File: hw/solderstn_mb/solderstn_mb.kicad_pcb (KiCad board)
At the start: 4 copper layers, 160 x 221.5 mm, 411 parts, among them J1201 Conn_02x05_Odd_Even, J1202 USB_B-TE_1734346-1, J1203 DB9_Male_MountingHoles, J1204 USB_A-CUI-UJ2-AH-1-SMT, J1205 Molex_NanoFit-1x02, J1301 SJ-3571N, J1302 Conn_02x05_Odd_Even, J201 74980104400, J2101 Conn_01x02, J2102 Molex_PicoBlade-53398-0271, J2103 CES-30207-158L120-67_Molex-Pi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, J2104 CES-703116-28PM_JST-conn, J2105 CES-30207-158L120-67_Molex-Pi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, J2106 CES-703116-28PM_JST-conn, J2107 Conn_Coaxial, J301 Molex_MicroFit_30-43045-0421, J501 FFC_conn_14p, J502 FFC_conn_14p, J503 JST_S2B-PH-SM4-TB, M501 FFC_retention_clamp, M502 FFC_retention_clamp, M601 Fan_4pin, M701 Fan_4pin, M801 Fan_4pin, Q1601 DMG1013T, Q1701 DMG1013T, Q1901 DMG1013T, Q2001 DMG1013T, Q2201 DMG1012T, Q301 Si4497DY, Q302 Si4497DY, Q303 DMG1012T, Q501 DMG1012T, Q601 DMG1012T, Q701 DMG1012T, Q801 DMG1012T, SW2201 Pushbutton_SMD_TS-1102W-4316, SW2202 Pushbutton_SMD_TS-1102W-4316, U1001 TMP100, U1101 TMP100, U1201 USBLC6-2SC6, U1202 74LVC2G17gw, U1203 USBLC6-2SC6, U1401 TMUX1219, U1402 TMUX1219, U1501 AD8552ARU, U1502 INA226, U1503 TPS2HB16AQ1, U1504 INA226, U1505 74LVC1G11dck, U1506 74LVC1G11dck, U1507 74LVC1G11dck, U1601 NE556d, U1602 74LVC1G175dck, U1603 74LVC1G11dck, U1701 74LVC1G175dck, U1702 74LVC1G11dck, U1801 AD8552ARU, U1802 INA226, U1803 TPS2HB16AQ1, U1804 INA226, U1805 74LVC1G11dck, U1806 74LVC1G11dck, U1807 74LVC1G11dck, U1901 NE556d, U1902 74LVC1G175dck, U1903 74LVC1G11dck, U2001 74LVC1G175dck, U2002 74LVC1G11dck, U201 IP101GA, U202 74LVC1G126SE, U2101 Si4735-D60-GU, U2102 TS4990IDT, U2103 TS4990IDT, U2201 MCP1316T-26LE-OT, U2202 W25Q64FV, U301 TPS54332DDA, U302 TLV1117LV30DCY, U303 TLV1117LV30DCY, U304 TLV1117LV30DCY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

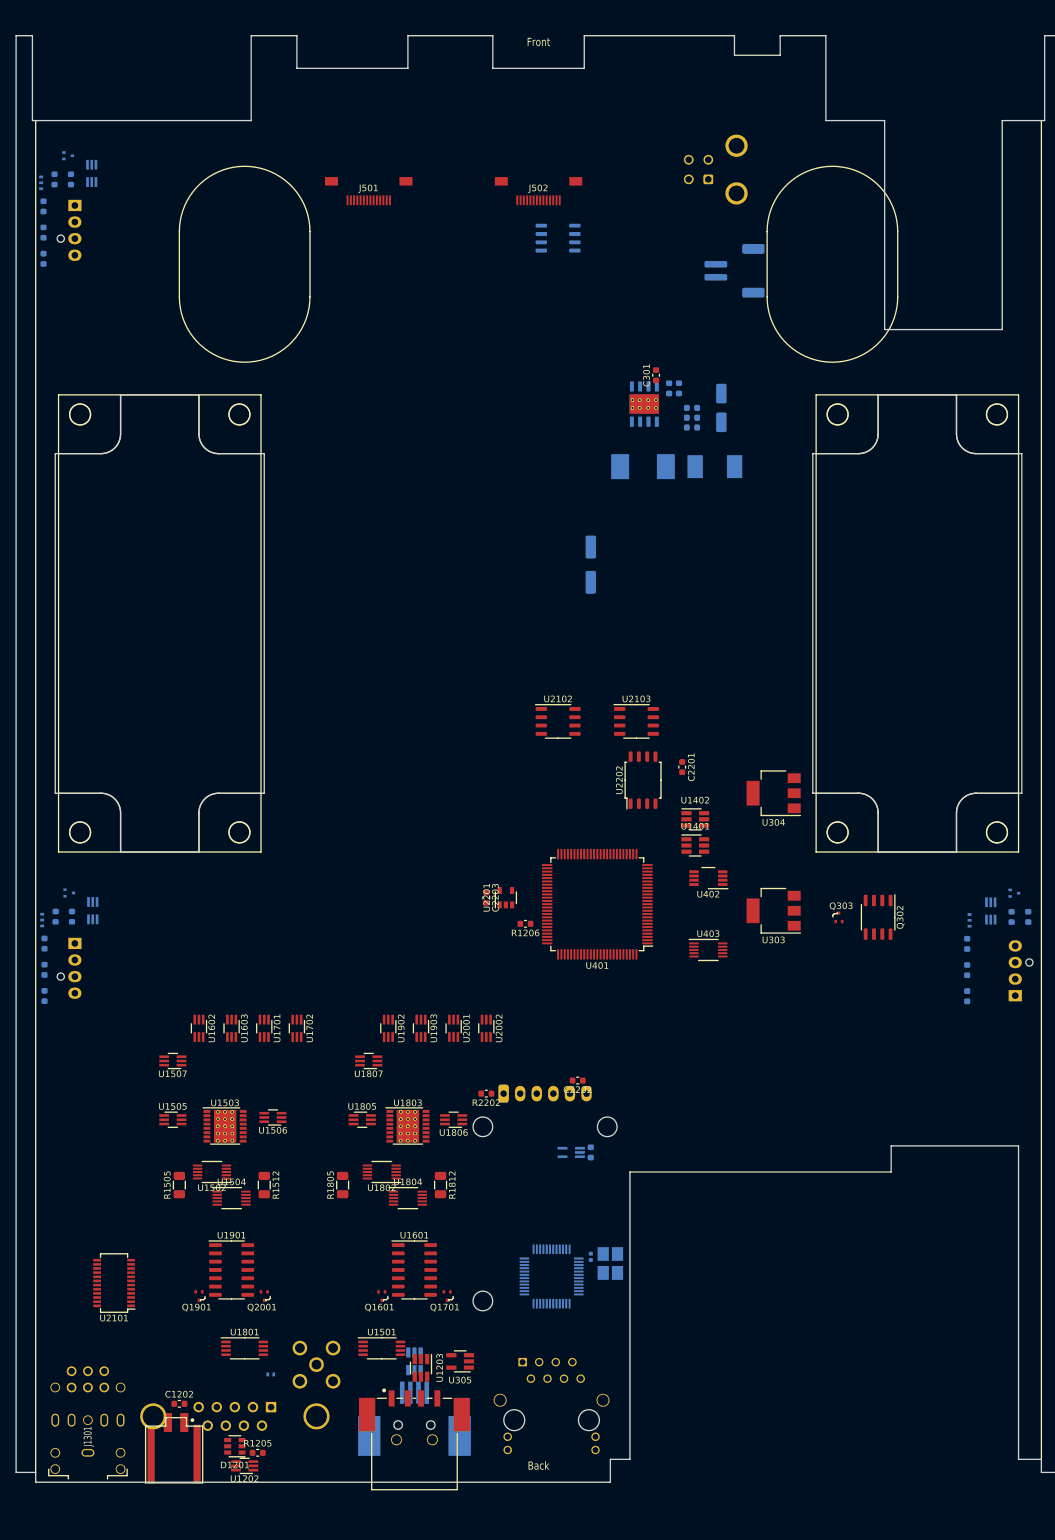
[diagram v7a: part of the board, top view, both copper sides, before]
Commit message: Rearpanel: IDC 2x5 instead of Dsub9 as dbg/bootstrp conn. Remove secondary fuseholder; rearrange DIN, P.E. banana, dbg. for more space. MainBoard: Rotate MW PSU 180deg (optimize for 230V through PwrBtn). PCB-fuse for 12V secondary side. IDC 2x5 instead of Dsub9; include DbgLED on free pin; ESD TVS on all dbgcon pins
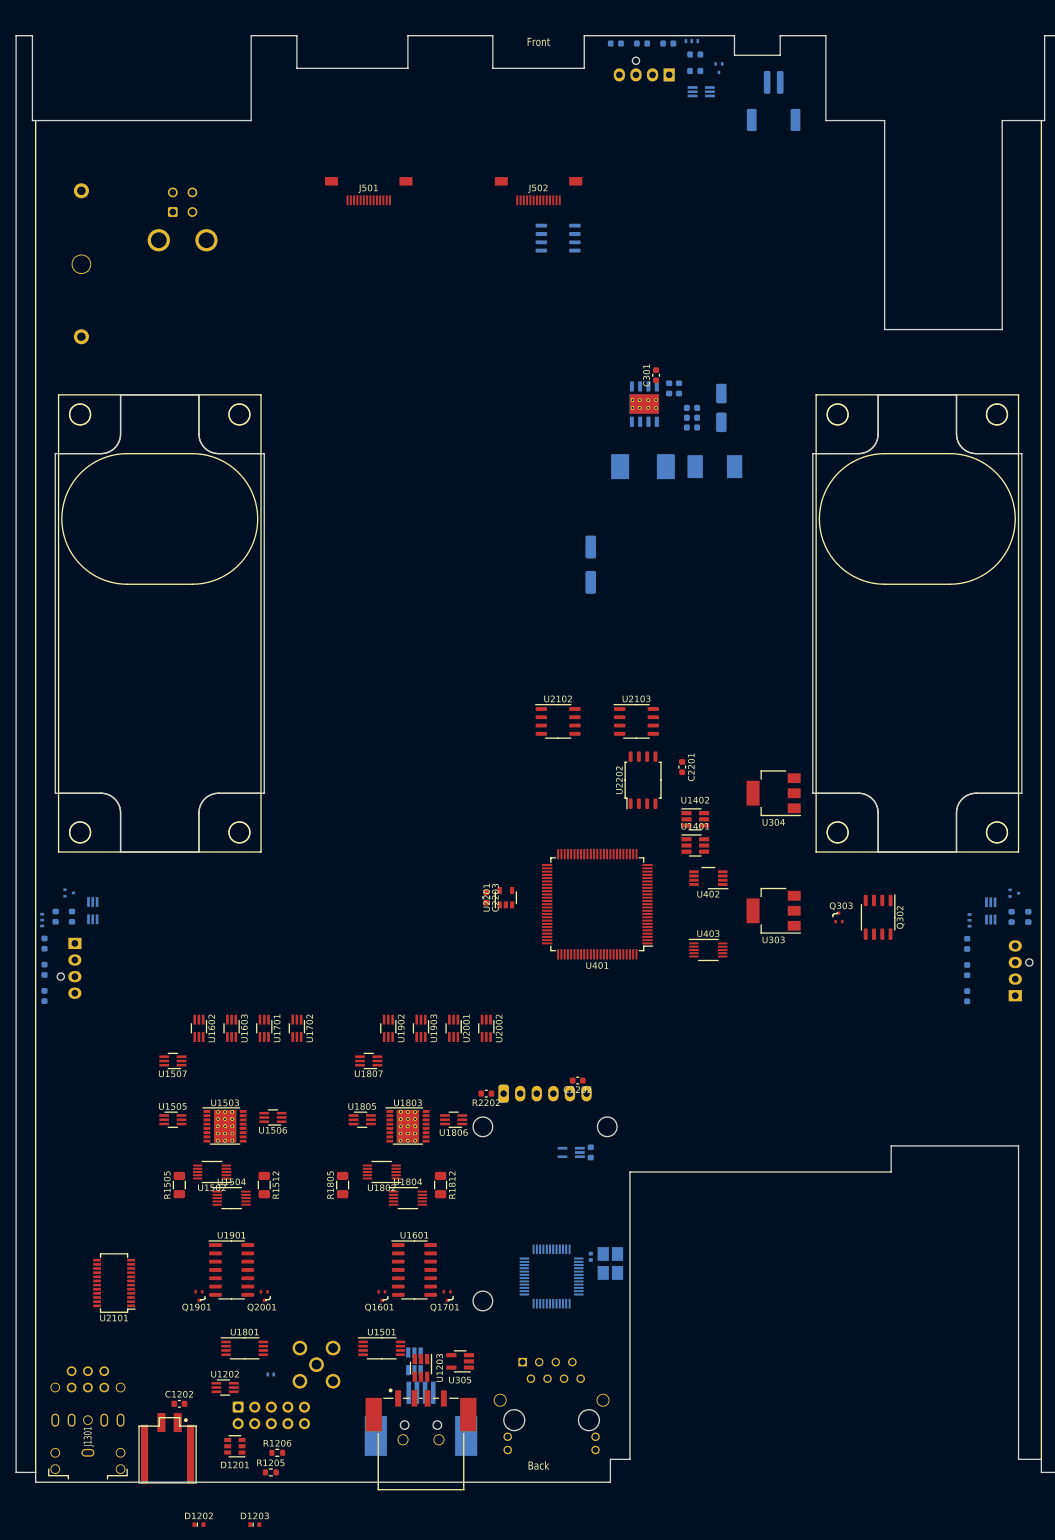
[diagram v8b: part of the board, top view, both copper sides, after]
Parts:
- added D1202: SLESD5Z5V, customlib_mj_fp:D_SOD-523, F.Cu at (98.0, 258.0)
- added D1203: SLESD5Z5V, customlib_mj_fp:D_SOD-523, F.Cu at (106.5, 258.0)
- added F301: Fuse_12V_5A, customlib_mj_fp:Fuseholder_5x20mm_Schurter_OGN-0031.8201, B.Cu at (80.0, 65.0)
- J1203: value DB9_Male_MountingHoles -> IDC_2x5; footprint customlib_mj_fp:DSub9-Kycon_K22X-EP9P-N -> Connector_IDC:IDC-Header_2x05_P2.54mm_Horizontal
- moved JP701 102.0 mm to (173.5, 30.8), turned to 0 degrees
- moved Q701 100.5 mm to (177.6, 35.0), turned to 0 degrees
- moved C701 99.9 mm to (174.0, 32.9), turned to 0 degrees
- moved C702 98.9 mm to (169.9, 31.2), turned to 0 degrees
- moved R702 97.0 mm to (174.0, 35.4), turned to 0 degrees
- moved R703 96.1 mm to (165.8, 31.2), turned to 0 degrees
- moved U701 94.2 mm to (174.9, 38.6), turned to 0 degrees
- moved R701 93.6 mm to (161.8, 31.2), turned to 0 degrees
- moved M701 93.2 mm to (170.0, 36.0), turned to 180 degrees
- moved R1206 89.5 mm to (110.0, 247.0), turned to 0 degrees
- moved J301 82.2 mm to (94.0, 57.0), turned to 0 degrees
- moved LS2101 41.1 mm to (92.0, 104.0), turned to 90 degrees
- moved LS2103 41.1 mm to (208.0, 104.0), turned to 270 degrees
- moved J503 26.7 mm to (186.0, 40.0), turned to 180 degrees
- moved U1202 12.4 mm to (102.0, 237.0), turned to 0 degrees
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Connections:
- D1201 pad 3: SWDIO -> Net-(D1201-Pad3)
- D1201 pad 4: SWCLK -> ~EXT_RSTn~
- D1201 pad 5: MCU_BOOT0 -> SWDIO
- D1201 pad 6: Net-(D1201-Pad6) -> SWCLK
- D2201 pad 1: Net-(D2201-Pad1) -> DBGLEDn
- J1203 pad 1: ~EXT_RSTn~ -> VCC
- J1203 pad 2: Net-(D1201-Pad1) -> GND
- J1203 pad 3: Net-(D1201-Pad6) -> MCU_BOOT0
- J1203 pad 4: MCU_BOOT0 -> SWCLK
- J1203 pad 5: VCC -> Net-(D1201-Pad1)
- J1203 pad 6: GND -> DBGLEDn
- J1203 pad 7: SWDIO -> Net-(D1201-Pad3)
- J1203 pad 8: SWCLK -> SWDIO
- J1203 pad 9: GND -> ~EXT_RSTn~
- Q2201 pad 3: Net-(D2201-Pad1) -> DBGLEDn
- Q301 pad 5: +VDC -> Net-(F301-Pad2)
- Q301 pad 6: +VDC -> Net-(F301-Pad2)
- Q301 pad 7: +VDC -> Net-(F301-Pad2)
- Q301 pad 8: +VDC -> Net-(F301-Pad2)
- R1205 pad 1: Net-(R1205-Pad1) -> DBGUART_RX
- R1205 pad 2: Net-(D1201-Pad6) -> Net-(R1205-Pad2)
- R1206 pad 1: DBGUART_RX -> Net-(D1201-Pad3)
- U1202 pad 1: DBGUART_TX -> Net-(D1201-Pad1)
- U1202 pad 2: GND -> VCC
- U1202 pad 3: Net-(D1201-Pad1) -> DBGUART_TX
- U1202 pad 5: VCC -> GND
- U1202 pad 6: Net-(R1205-Pad1) -> Net-(R1205-Pad2)
